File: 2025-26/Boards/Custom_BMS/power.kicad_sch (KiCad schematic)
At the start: 26 parts, among them J2 Conn_01x02_Pin, Q2 AO3401A, U2 TPS563300, U4 AMS1117-3.3

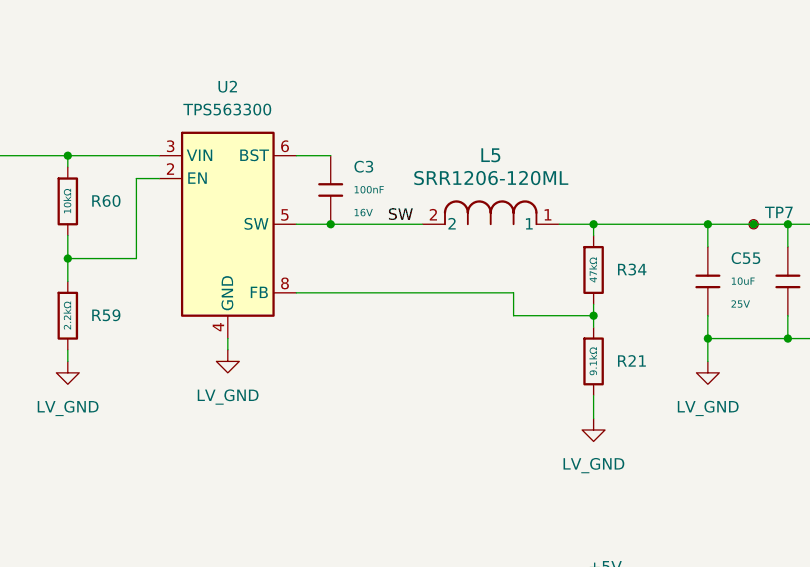
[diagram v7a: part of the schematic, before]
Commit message: started edits after PI suggestions
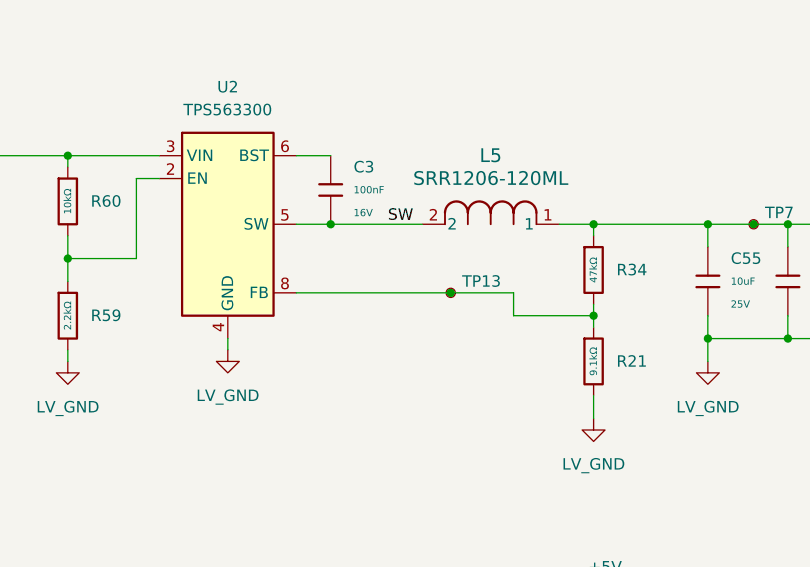
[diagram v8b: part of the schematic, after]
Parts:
- added TP13: TestPoint_Small, TestPoint:TestPoint_Pad_D1.0mm, symbol Connector:TestPoint_Small
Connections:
- net at R21.1, R34.2, U2.8 (FB): now also TP13.1
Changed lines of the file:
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@@
 	)
 	(junction
+		(at 121.285 87.63)
+		(diameter 0)
+		(color 0 0 0 0)
+	)
+	(junction
 		(at 107.95 80.01)
 		(diameter 0)
@@
 	(wire
 		(pts
+			(xy 121.285 87.63) (xy 128.27 87.63)
+		)
+		(stroke
+			(width 0)
+			(type default)
+		)
+	)
+	(wire
+		(pts
 			(xy 100.33 133.35) (xy 110.49 133.35)
 		)
@@
 	(wire
 		(pts
-			(xy 104.14 87.63) (xy 128.27 87.63)
+			(xy 104.14 87.63) (xy 121.285 87.63)
 		)
 		(stroke
@@
 			"m28L0WnIyMgYM2aMchkGg3HlyhV3d3ftqITQLWiSiGjv1NTUSDa6twaVSh06dKi0PwvRiUFmC4FA"
 			"dDCQbwuBQHQwkNlCIBAdDGS2EAhEBwOZLQQC0cFAZguBQHQwkNlCIBAdDGS2EAhEBwOZLQQC0cFA"
-			"ZguBQHQwkNlCIBAdDGS2EAhEBwOZLQQC0cFAZguBQHQw/h8X1ozGxq4eFwAAAABJRU5ErkJggg=="
+			"ZguBQHQwkNlCIBAdDGS2EAhEBwOZLQQC0cFAZguBQHQw/h8X1ozGxq4eFwAAAABJRU5ErkJgggQA"
+			"AAAEAAAABAAAAAQAAAAEAAAABAAAAAQAAAAEAAAABAAAAAQAAAAEAAAABAAAAAQAAAAEAAAABAAA"
+			"AAQAAAAEAAAABAAAAAQAAAAEAAAABAAAAAQAAAAEAAAABAAAAAQAAAAEAAAABAAAAAQAAAAEAAAA"
+			"BAAAAAQAAAAEAAAABAAAAAQAAAAEAAAABAAAAAQAAAAEAAAABAAAAAQAAAAEAAAABAAAAAQAAAAE"
+			"AAAABAAAAAQAAAAEAAAABAAAAAQAAAAEAAAABAAAAAQAAAAEAAAABAAAAAQAAAAEAAAABAAAAAQA"
+			"AAAEAAAABAAAAAQAAAAEAAAABAAAAAQAAAAEAAAABAAAAAQAAAAEAAAABAAAAAQAAAAEAAAABAAA"
+			"AAQAAAAEAAAABAAAAAQAAAAEAAAABAAAAAQAAAAEAAAABAAAAAQAAAAEAAAABAAAAAQAAAAEAAAA"
+			"BAAAAAQAAAAEAAAABAAAAAQAAAAEAAAABAAAAAQAAAAEAAAABAAAAAQAAAAEAAAABAAAAAQAAAAE"
+			"AAAABAAAAAQAAAAEAAAABAAAAAQAAAAEAAAABAAAAAQAAAAEAAAABAAAAAQAAAAEAAAABAAAAAQA"
+			"AAAEAAAABAAAAAQAAAAEAAAABAAAAAQAAAAEAAAABAAAAAQAAAAEAAAABAAAAAQAAAAEAAAABAAA"
+			"AAQAAAAEAAAABAAAAAQAAAAEAAAABAAAAAQAAAAEAAAABAAAAAQAAAAEAAAABAAAAAQAAAAEAAAA"
+			"BAAAAAQAAAAEAAAABAAAAAQAAAAEAAAABAAAAAQAAAAEAAAABAAAAAQAAAAEAAAABAAAAAQAAAAE"
+			"AAAABAAAAAQAAAAEAAAABAAAAAQAAAAEAAAABAAAAAQAAAAEAAAABAAAAAQAAAAEAAAABAAAAAQA"
+			"AAAEAAAABAAAAAQAAAAEAAAABQAAAAcAAAAHAAAAAQAAAAAAAAAAAAAAAAAAAAAAAAAFAAAABwAA"
+			"AAcAAAAHAAAABwAAAAcAAAAHAAAABwAAAAcAAAAHAAAABwAAAAcAAAAHAAAABwAAAAcAAAAHAAAA"
+			"BwAAAAcAAAAHAAAABwAAAAcAAAAHAAAABwAAAAcAAAAHAAAABwAAAAcAAAAHAAAABwAAAAcAAAAH"
+			"AAAABwAAAAcAAAAHAAAABwAAAAcAAAAHAAAABwAAAAcAAAAHAAAABwAAAAcAAAAHAAAABwAAAAcA"
+			"AAAHAAAABwAAAAcAAAAHAAAABwAAAAcAAAAHAAAABwAAAAcAAAAHAAAABwAAAAcAAAAHAAAABwAA"
+			"AAcAAAAHAAAABwAAAAcAAAAHAAAABwAAAAcAAAAHAAAABwAAAAcAAAAHAAAABwAAAAcAAAAHAAAA"
+			"BwAAAAcAAAAHAAAABwAAAAcAAAAHAAAABwAAAAcAAAAHAAAABwAAAAcAAAAHAAAABwAAAAcAAAAH"
+			"AAAABwAAAAcAAAAHAAAABwAAAAcAAAAHAAAABwAAAAcAAAAHAAAABwAAAAcAAAAHAAAABwAAAAcA"
+			"AAAHAAAABwAAAAcAAAAHAAAABwAAAAcAAAAHAAAABwAAAAcAAAAHAAAABwAAAAcAAAAHAAAABwAA"
+			"AAcAAAAHAAAABwAAAAcAAAAHAAAABwAAAAcAAAAHAAAABwAAAAcAAAAHAAAABwAAAAcAAAAHAAAA"
+			"BwAAAAcAAAAHAAAABwAAAAcAAAAHAAAABwAAAAcAAAAHAAAABwAAAAcAAAAHAAAABwAAAAcAAAAH"
+			"AAAABwAAAAcAAAAHAAAABwAAAAcAAAAHAAAABwAAAAcAAAAHAAAABwAAAAcAAAAHAAAABwAAAAcA"
+			"AAAHAAAABwAAAAcAAAAHAAAABwAAAAcAAAAHAAAABwAAAAcAAAAHAAAABwAAAAcAAAAHAAAABwAA"
+			"AAcAAAAHAAAABwAAAAcAAAAHAAAABwAAAAcAAAAHAAAABwAAAAcAAAAHAAAABwAAAAcAAAAHAAAA"
+			"BwAAAAcAAAAHAAAABwAAAAcAAAAHAAAABwAAAAcAAAAHAAAABwAAAAcAAAAHAAAABwAAAAcAAAAH"
+			"AAAABwAAAAcAAAAHAAAABwAAAAcAAAAHAAAABwAAAAcAAAAHAAAABwAAAAcAAAAHAAAABwAAAAcA"
+			"AAAHAAAABwAAAAcAAAAHAAAABwAAAAcAAAAHAAAABwAAAAcAAAAHAAAABwAAAAcAAAAHAAAABwAA"
+			"AAcAAAAHAAAABwAAAAcAAAAHAAAABwAAAAcAAAAHAAAABwAAAAcAAAAHAAAABwAAAAcAAAAHAAAA"
+			"BwAAAAcAAAAHAAAABwAAAAcAAAAFAAAAAAAAAAAAAAAAAAAAAAAAAAAAAAAAAAAAAAAAAAAAAAAA"
+			"AAAAAAAAAAAAAAAAAAAAAAAAAAAAAAAAAAAAAAAAAAAAAAAAAAAAAAAAAAAAAAAAAAAAAAAAAAAA"
+			"AAAAAAAAAAAAAAAAAAAAAAAAAAAAAAAAAAAAAAAAAAAAAAAAAAAAAAAAAAAAAAAAAAAAAAAAAAAA"
+			"AAAAAAAAAAAAAAAAAAAAAAAAAAAAAAAAAAAAAAAAAAAAAAAAAAAAAAAAAAAAAAAAAAAAAAAAAAAA"
+			"AAAAAAAAAAAAAAAAAAAAAAAAAAAAAAAAAAAAAAAAAAAAAAAAAAAAAAAAAAAAAAAAAAAAAAAAAAAA"
+			"AAAAAAAAAAAAAAAAAAAAAAAAAAAAAAAAAAAAAAAAAAAAAAAAAAAAAAAAAAAAAAAAAAAAAAAAAA=="
 		)
 	)
@@
 			"Mf5TIpF4eXkRYyzLy8uzs7Px0FYMw8zMzIYNG0Z8UEJCAmwE2TYEAoGQR0vbhmi3oPU2BAKBQBga"
 			"yLYhEAgEwtBAtg2BQCAQhgaybQgEAoEwNJBtQyAQCHloNBoMDkR0UJBtQyAQCHm6dOlSU1Ojqmo+"
-			"ov2DbBsCgUDIY2FhQSaTYQJZW+uCaA7/D/QaWdC9vkuXAAAAAElFTkSuQmCC"
+			"ov2DbBsCgUDIY2FhQSaTYQJZW+uCaA7/D/QaWdC9vkuXAAAAAElFTkSuQmCCAAAAAAAAAAAAAAAA"
+			"AAAAAAAAAAAAAAAAAAAAAAAAAAAAAAAAAAAAAAAAAAAAAAAAAAAAAAAAAAAAAAAAAAAAAAAAAAAA"
+			"AAAAAAAAAAAAAAAAAAAAAAAAAAAAAAAAAAAAAAAAAAAAAAAAAAAAAAAAAAAAAAAAAAAAAAAAAAAA"
+			"AAAAAAAAAAAAAAAAAAAAAAAAAAAAAAAAAAAAAAAAAAAAAAAAAAAAAAAAAAAAAAAAAAAAAAAAAAAA"
+			"AAAAAAAAAAAAAAAAAAAAAAAAAAAAAAAAAAAAAAAAAAAAAAAAAAAAAAAAAAAAAAAAAAAAAAAAAAAA"
+			"AAACAAAAAAAAAAAAAAAAAAAAAAAAAAAAAAAAAAAAAAAAAAAAAAAAAAAAAAAAAAAAAAAAAAAAAAAA"
+			"AAAAAAAAAAAAAAAAAAAAAAAAAAAAAAAAAAAAAAAAAAAAAAAAAAAAAAAAAAAAAAAAAAAAAAAAAAAA"
+			"AAAAAAAAAAAAAAAAAAAAAAAAAAAAAAAAAAAAAAAAAAAAAAAAAAAAAAAAAAAAAAAAAAAAAAAAAAAA"
+			"AAAAAAAAAAAAAAAAAAAAAAAAAAAAAAAAAAAAAAAAAAAAAAAAAAAAAAAAAAAAAAAAAAAAAAAAAAAA"
+			"AAAAAAAAAAAAAAAAAAAAAAAAAAAAAAAAAAAAAAAAAAAAAAAAAAAAAAAAAAAAAAAAAAAAAAAAAAAA"
+			"AAAAAAAAAAAAAAAAAAAAAAAAAAAAAAAAAAAAAAAAAAAAAAAAAAAAAAAAAAAAAAAAAAAAAAAAAAAA"
+			"AAAAAAAAAAAAAAAAAAAAAAAAAAAAAAAAAAAAAAAAAAAAAAAAAAAAAAAAAAAAAAAAAAAAAAAAAAAA"
+			"AAAAAAAAAAAAAAAAAAAAAAAAAAAAAAAAAAAAAAAAAAAAAAAAAAAAAAAAAAAAAAAAAAAAAAAAAAAA"
+			"AAAAAAAAAAAAAAAAAAAAAAAAAAAAAAAAAAAAAAAAAAAAAAAAAAAAAAAAAAAAAAAAAAAAAAAAAAAA"
+			"AAAAAAAAAAAAAAAAAAAAAAAAAAAAAAAAAAAAAAAAAAAAAAAAAAAAAAAAAAAAAAAAAAAAAAAAAAAA"
+			"AAAAAAAAAAAAAAAAAAAAAAAAAAAAAAAAAAAAAAAAAAAAAAAAAAAAAAAAAAAAAAAAAAAAAAAAAAAA"
+			"AAAAAAAAAAAAAAAAAAAAAAAAAAAAAAAAAAAAAAAAAAAAAAAAAAAAAAAAAAAAAAAAAAAAAAAAAAAA"
+			"AAAAAAAAAAAAAAAAAAAAAAAAAAAAAAAAAAAAAAAAAAAAAAAAAAAAAAAAAAAAAAAAAAAAAAAAAAAA"
+			"AAAAAAAAAAAAAAAAAAAAAAAAAAAAAAAAAAAAAAAAAAAAAAAAAAAAAAAAAAAAAAAAAAAAAAAAAAAA"
+			"AAAAAAAAAAAAAAAAAAAAAAAAAAAAAAAAAAAAAAAAAAAAAAAAAAAAAAAAAAAAAAAAAAAAAAAAAAAA"
+			"AAAAAAAAAAAAAAAAAAAAAAAAAAAAAAAAAAAAAAAAAAAAAAAAAAAAAAAAAAAAAAAAAAAAAAAAAAAA"
+			"AAAAAAAAAAAAAAAAAAAAAAAAAAAAAAAAAAAAAAAAAAAAAAAAAAAAAAAAAAAAAAAAAAAAAAAAAAAA"
+			"AAAAAAAAAAAAAAAAAAAAAAAAAAAAAAAAAAAAAAAAAAAAAAAAAAAAAAAAAAAAAAAAAAAAAAAAAAAA"
+			"AAAAAAAAAAAAAAAAAAAAAAAAAAAAAAAAAAAAAAAAAAAAAAAAAAAAAAAAAAAAAAAAAAAAAAAAAAAA"
+			"AAAAAAAAAAAAAAAAAAAAAAAAAAAAAAAAAAAAAAAAAAAAAAAAAAAAAAAAAAAAAAAAAAAAAAAAAAAA"
+			"AAAAAAAAAAAAAAAAAAAAAAAAAAAAAAAAAAAAAAAAAAAAAAAAAAAAAAAAAAAAAAAAAAAAAAAAAAAA"
+			"AAAAAAAAAAAAAAAAAAAAAAAAAAAAAAAAAAAAAAAAAAAAAAAAAAAAAAAAAAAAAAAAAAAAAAAAAAAA"
+			"AAAAAAAAAAAAAAAAAAAAAAAAAAAAAAAAAAAAAAAAAAAAAAAAAAAAAAAAAAAAAAAAAAAAAAAAAAAA"
+			"AAAAAAAAAAAAAAAAAAAAAAAAAAAAAAAAAAAAAAAAAAAAAAAAAAAAAAAAAAAAAAAAAAAAAAAAAAAA"
+			"AAAAAAAAAAAAAAAAAAAAAAAAAAAAAAAAAAAAAAAAAAAAAAAAAAAAAAAAAAAAAAAAAAAAAAAAAAAA"
+			"AAAAAAAAAAAAAAAAAAAAAAAAAAAAAAAAAAAAAAAAAAAAAAAAAAAAAAAAAAAAAAAAAAAAAAAAAAAA"
+			"AAAAAAAAAAAAAAAAAAAAAAAAAAAAAAAAAAAAAAAAAAAAAAAAAAAAAAAAAAAAAAAAAAAAAAAAAAAA"
+			"AAAAAAAAAAAAAAAAAAAAAAAAAAAAAAAAAAAAAAAAAAAAAAAAAAAAAAAAAAAAAAAAAAAAAAAAAAAA"
+			"AAAAAAAAAAAAAAAAAAAAAAAAAAAAAAAAAAAAAAAAAAAAAAAAAAAAAAAAAAAAAAAAAAAAAAAAAAAA"
+			"AAAAAAAAAAAAAAAAAAAAAAAAAAAAAAAAAAAAAAAAAAAAAAAAAAAAAAAAAAAAAAAAAAAAAAAAAAAA"
+			"AAAAAAAAAAAAAAAAAAAAAAAAAAAAAAAAAAAAAAAAAAAAAAAAAAAAAAAAAAAAAAAAAAAAAAAAAAAA"
+			"AAAAAAAAAAAAAAAAAAAAAAAAAAAAAAAAAAAAAAAAAAAAAAAAAAAAAAAAAA=="
 		)
 	)
@@
 					(unit 1)
 				)
+			)
+		)
+	)
+	(symbol
+		(lib_id "Connector:TestPoint_Small")
+		(at 121.285 87.63 0)
+		(unit 1)
+		(exclude_from_sim no)
+		(in_bom yes)
+		(on_board yes)
+		(dnp no)
+		(fields_autoplaced yes)
+		(property "Reference" "TP13"
+			(at 122.555 86.3599 0)
+			(effects
+				(font
+					(size 1.27 1.27)
+				)
+				(justify left)
+			)
+		)
+		(property "Value" "TestPoint_Small"
+			(at 122.555 88.8999 0)
+			(effects
+				(font
+					(size 1.27 1.27)
+				)
+				(justify left)
+				(hide yes)
+			)
+		)
+		(property "Footprint" "TestPoint:TestPoint_Pad_D1.0mm"
+			(at 126.365 87.63 0)
+			(effects
+				(font
+					(size 1.27 1.27)
+				)
+				(hide yes)
+			)
+		)
+		(property "Datasheet" "~"
+			(at 126.365 87.63 0)
+			(effects
+				(font
+					(size 1.27 1.27)
+				)
+				(hide yes)
+			)
+		)
+		(property "Description" "test point"
+			(at 121.285 87.63 0)
+			(effects
+				(font
+					(size 1.27 1.27)
+				)
+				(hide yes)
+			)
+		)
+		(pin "1"
+		)
+		(instances
+			(project "Custom_BMS"
+				(path "/570d6d9c-ebf5-4f83-96f6-d3309a3e637d/ac1bd3bc-1261-453f-909d-f00789f9c421"
+					(reference "TP13")
+					(unit 1)
+				)
